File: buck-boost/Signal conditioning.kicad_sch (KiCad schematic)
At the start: 11 parts, among them U10 Opamp_Dual, U13 Opamp_Dual

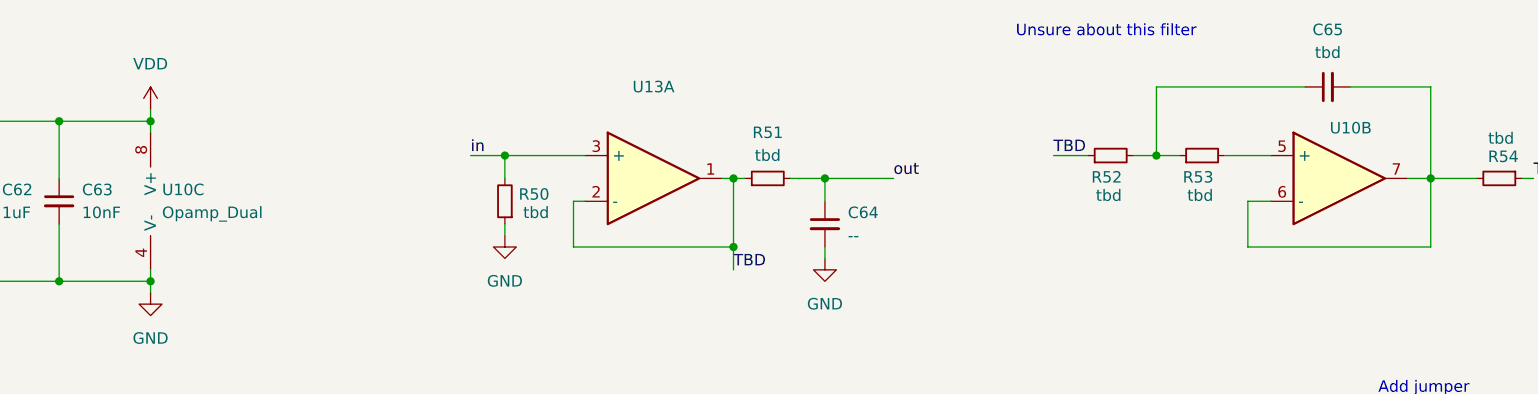
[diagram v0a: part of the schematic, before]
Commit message: Editing sheets(Power labels, sheet color, adding text), Adding information in the sensor sheets
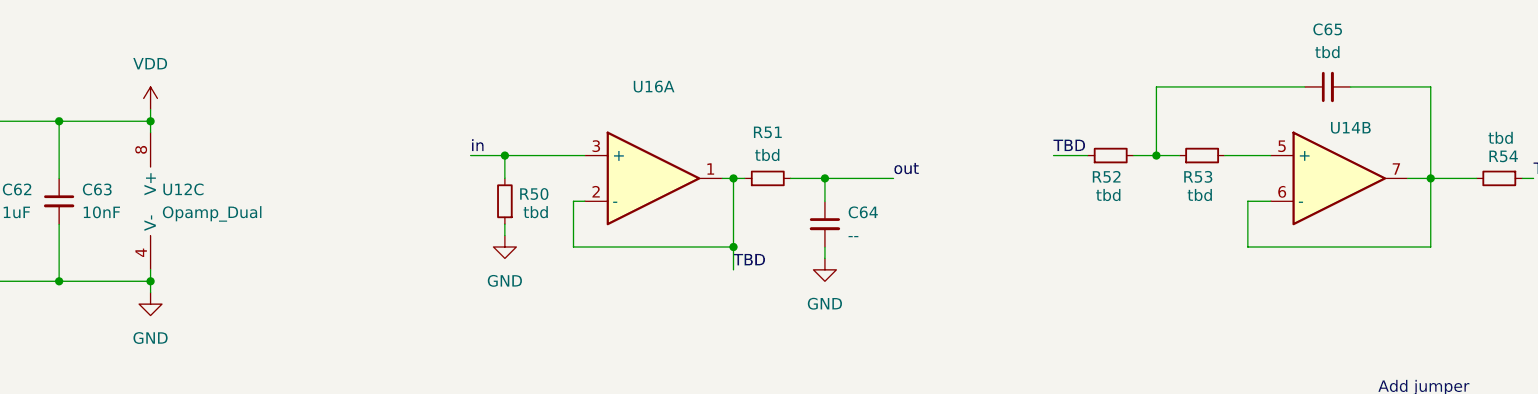
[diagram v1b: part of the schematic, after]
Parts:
- renumbered U10 to U12, U10 to U14, U13 to U16
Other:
- note removed: "Unsure about this filter"
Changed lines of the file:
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@@
 		)
 	)
-	(text "Unsure about this filter\n"
-		(exclude_from_sim no)
-		(at 156.972 39.624 0)
+	(label "in"
+		(at 22.86 177.8 0)
+		(fields_autoplaced yes)
 		(effects
 			(font
 				(size 1.27 1.27)
-				(color 255 57 0 1)
-			)
+			)
+			(justify left bottom)
 		)
 	)
 	(label "in"
-		(at 22.86 177.8 0)
+		(at 86.36 53.34 0)
 		(fields_autoplaced yes)
 		(effects
@@
 		)
 	)
-	(label "in"
-		(at 86.36 53.34 0)
+	(label "TBD"
+		(at 151.13 53.34 0)
 		(fields_autoplaced yes)
 		(effects
@@
 		)
 	)
-	(label "TBD"
-		(at 151.13 53.34 0)
+	(label "out"
+		(at 46.99 177.8 0)
 		(fields_autoplaced yes)
 		(effects
@@
 		)
 	)
-	(label "out"
-		(at 46.99 177.8 0)
+	(label "TBD_filt"
+		(at 204.47 55.88 0)
 		(fields_autoplaced yes)
 		(effects
@@
 		)
 	)
-	(label "TBD_filt"
-		(at 204.47 55.88 0)
+	(label "TBD"
+		(at 115.57 66.04 0)
 		(fields_autoplaced yes)
 		(effects
@@
 		)
 	)
-	(label "TBD"
-		(at 115.57 66.04 0)
+	(label "out"
+		(at 133.35 55.88 0)
 		(fields_autoplaced yes)
 		(effects
@@
 		)
 	)
-	(label "out"
-		(at 133.35 55.88 0)
+	(hierarchical_label "in"
+		(shape input)
+		(at 25.4 177.8 0)
 		(fields_autoplaced yes)
 		(effects
@@
 				(size 1.27 1.27)
 			)
-			(justify left bottom)
-		)
-	)
-	(hierarchical_label "in"
-		(shape input)
-		(at 25.4 177.8 0)
+			(justify left)
+		)
+	)
+	(hierarchical_label "out"
+		(shape output)
+		(at 50.8 177.8 0)
 		(fields_autoplaced yes)
 		(effects
@@
 		)
 	)
-	(hierarchical_label "out"
-		(shape output)
-		(at 50.8 177.8 0)
-		(fields_autoplaced yes)
-		(effects
-			(font
-				(size 1.27 1.27)
-			)
-			(justify left)
-		)
-	)
 	(symbol
 		(lib_id "Device:R_Small")
@@
 					(unit 1)
 				)
-				(path "/3f994017-d36f-4c43-a8c8-740bd919e8ad/70cf8e5f-42f7-4af1-be5f-f7a395e09e78/4c95cbf9-e4e0-409d-a846-0f8d58b8f8d6/db151abd-a3a5-4ce2-8717-af92247b7384"
-					(reference "R43")
-					(unit 1)
-				)
 			)
 		)
@@
 					(unit 1)
 				)
-				(path "/3f994017-d36f-4c43-a8c8-740bd919e8ad/70cf8e5f-42f7-4af1-be5f-f7a395e09e78/4c95cbf9-e4e0-409d-a846-0f8d58b8f8d6/db151abd-a3a5-4ce2-8717-af92247b7384"
-					(reference "#PWR055")
-					(unit 1)
-				)
 			)
 		)
@@
 					(unit 1)
 				)
-				(path "/3f994017-d36f-4c43-a8c8-740bd919e8ad/70cf8e5f-42f7-4af1-be5f-f7a395e09e78/4c95cbf9-e4e0-409d-a846-0f8d58b8f8d6/db151abd-a3a5-4ce2-8717-af92247b7384"
-					(reference "#PWR029")
-					(unit 1)
-				)
 			)
 		)
@@
 		(on_board yes)
 		(dnp no)
-		(property "Reference" "U10"
+		(property "Reference" "U14"
 			(at 184.15 50.292 0)
 			(effects
@@
 				(path "/3f994017-d36f-4c43-a8c8-740bd919e8ad/70cf8e5f-42f7-4af1-be5f-f7a395e09e78/4c95cbf9-e4e0-409d-a846-0f8d58b8f8d6/95c7b7af-0b0f-47b5-89a1-4c64764014b4"
 					(reference "U13")
-					(unit 2)
-				)
-				(path "/3f994017-d36f-4c43-a8c8-740bd919e8ad/70cf8e5f-42f7-4af1-be5f-f7a395e09e78/4c95cbf9-e4e0-409d-a846-0f8d58b8f8d6/db151abd-a3a5-4ce2-8717-af92247b7384"
-					(reference "U10")
 					(unit 2)
 				)
@@
 					(unit 1)
 				)
-				(path "/3f994017-d36f-4c43-a8c8-740bd919e8ad/70cf8e5f-42f7-4af1-be5f-f7a395e09e78/4c95cbf9-e4e0-409d-a846-0f8d58b8f8d6/db151abd-a3a5-4ce2-8717-af92247b7384"
-					(reference "#PWR030")
-					(unit 1)
-				)
 			)
 		)
@@
 					(unit 1)
 				)
-				(path "/3f994017-d36f-4c43-a8c8-740bd919e8ad/70cf8e5f-42f7-4af1-be5f-f7a395e09e78/4c95cbf9-e4e0-409d-a846-0f8d58b8f8d6/db151abd-a3a5-4ce2-8717-af92247b7384"
-					(reference "R42")
-					(unit 1)
-				)
 			)
 		)
@@
 					(unit 1)
 				)
-				(path "/3f994017-d36f-4c43-a8c8-740bd919e8ad/70cf8e5f-42f7-4af1-be5f-f7a395e09e78/4c95cbf9-e4e0-409d-a846-0f8d58b8f8d6/db151abd-a3a5-4ce2-8717-af92247b7384"
-					(reference "C56")
-					(unit 1)
-				)
 			)
 		)
@@
 					(unit 1)
 				)
-				(path "/3f994017-d36f-4c43-a8c8-740bd919e8ad/70cf8e5f-42f7-4af1-be5f-f7a395e09e78/4c95cbf9-e4e0-409d-a846-0f8d58b8f8d6/db151abd-a3a5-4ce2-8717-af92247b7384"
-					(reference "C54")
-					(unit 1)
-				)
 			)
 		)
@@
 		(dnp no)
 		(fields_autoplaced yes)
-		(property "Reference" "U10"
+		(property "Reference" "U12"
 			(at 52.07 57.1499 0)
 			(effects
@@
 				(path "/3f994017-d36f-4c43-a8c8-740bd919e8ad/70cf8e5f-42f7-4af1-be5f-f7a395e09e78/4c95cbf9-e4e0-409d-a846-0f8d58b8f8d6/95c7b7af-0b0f-47b5-89a1-4c64764014b4"
 					(reference "U11")
-					(unit 3)
-				)
-				(path "/3f994017-d36f-4c43-a8c8-740bd919e8ad/70cf8e5f-42f7-4af1-be5f-f7a395e09e78/4c95cbf9-e4e0-409d-a846-0f8d58b8f8d6/db151abd-a3a5-4ce2-8717-af92247b7384"
-					(reference "U10")
 					(unit 3)
 				)
@@
 					(unit 1)
 				)
-				(path "/3f994017-d36f-4c43-a8c8-740bd919e8ad/70cf8e5f-42f7-4af1-be5f-f7a395e09e78/4c95cbf9-e4e0-409d-a846-0f8d58b8f8d6/db151abd-a3a5-4ce2-8717-af92247b7384"
-					(reference "C57")
-					(unit 1)
-				)
 			)
 		)
@@
 					(unit 1)
 				)
-				(path "/3f994017-d36f-4c43-a8c8-740bd919e8ad/70cf8e5f-42f7-4af1-be5f-f7a395e09e78/4c95cbf9-e4e0-409d-a846-0f8d58b8f8d6/db151abd-a3a5-4ce2-8717-af92247b7384"
-					(reference "#PWR?")
-					(unit 1)
-				)
 			)
 		)
@@
 					(unit 1)
 				)
-				(path "/3f994017-d36f-4c43-a8c8-740bd919e8ad/70cf8e5f-42f7-4af1-be5f-f7a395e09e78/4c95cbf9-e4e0-409d-a846-0f8d58b8f8d6/db151abd-a3a5-4ce2-8717-af92247b7384"
-					(reference "C55")
-					(unit 1)
-				)
 			)
 		)
@@
 					(unit 1)
 				)
-				(path "/3f994017-d36f-4c43-a8c8-740bd919e8ad/70cf8e5f-42f7-4af1-be5f-f7a395e09e78/4c95cbf9-e4e0-409d-a846-0f8d58b8f8d6/db151abd-a3a5-4ce2-8717-af92247b7384"
-					(reference "R44")
-					(unit 1)
-				)
 			)
 		)
@@
 		(dnp no)
 		(fields_autoplaced yes)
-		(property "Reference" "U13"
+		(property "Reference" "U16"
 			(at 106.68 45.72 0)
 			(effects
@@
 				(path "/3f994017-d36f-4c43-a8c8-740bd919e8ad/70cf8e5f-42f7-4af1-be5f-f7a395e09e78/4c95cbf9-e4e0-409d-a846-0f8d58b8f8d6/95c7b7af-0b0f-47b5-89a1-4c64764014b4"
 					(reference "U15")
-					(unit 1)
-				)
-				(path "/3f994017-d36f-4c43-a8c8-740bd919e8ad/70cf8e5f-42f7-4af1-be5f-f7a395e09e78/4c95cbf9-e4e0-409d-a846-0f8d58b8f8d6/db151abd-a3a5-4ce2-8717-af92247b7384"
-					(reference "U13")
 					(unit 1)
 				)
@@
 					(unit 1)
 				)
-				(path "/3f994017-d36f-4c43-a8c8-740bd919e8ad/70cf8e5f-42f7-4af1-be5f-f7a395e09e78/4c95cbf9-e4e0-409d-a846-0f8d58b8f8d6/db151abd-a3a5-4ce2-8717-af92247b7384"
-					(reference "R40")
-					(unit 1)
-				)
 			)
 		)
@@
 					(unit 1)
 				)
-				(path "/3f994017-d36f-4c43-a8c8-740bd919e8ad/70cf8e5f-42f7-4af1-be5f-f7a395e09e78/4c95cbf9-e4e0-409d-a846-0f8d58b8f8d6/db151abd-a3a5-4ce2-8717-af92247b7384"
-					(reference "R41")
-					(unit 1)
-				)
